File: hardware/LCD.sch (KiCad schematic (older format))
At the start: 31 parts, among them IC1 TPS61169DCKR, IC2 TPD4E001DRLR, IC3 AR1021-I/SS, U3 DS90CF364AMTD

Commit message: Assigning footprints
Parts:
- removed TOUCH1: HSMY-C170, EEZ DIB MCU r1B1:LED_0805, symbol LCD_PMOD-rescue:LED0805-EEZ_DIB_MCU_r1B2-eagle-import
- added TOUCH1: LED, LED_SMD:LED_0603_1608Metric, symbol antena:LED
- C1: footprint EEZ DIB MCU r1B1:C1206 -> Capacitor_SMD:C_1206_3216Metric
- C10, C11, C12, C13, C14, C15, C16, C9: renamed from C?; footprint (none) -> Capacitor_SMD:C_0603_1608Metric
- C2, C7: footprint EEZ DIB MCU r1B1:C0603 -> Capacitor_SMD:C_0603_1608Metric
- C3, C4, C5, C6, C8: footprint EEZ DIB MCU r1B1:C0805 -> Capacitor_SMD:C_0805_2012Metric
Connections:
- net 3V3: now also C2.2, C5.1, C7.2, C8.2, IC2.6 (VCC), IC3.1 (VDD), LCD_OUT1.4 (VDD), R3.2
- net 5V: now reaches C1.1, L1.1, R1.1
- net at R5.1: now also TOUCH1.2 (A)
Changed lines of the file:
@@
 	3300 1100 3400 1100
 Wire Wire Line
-	4600 2000 3900 2000
+	4600 2000 4550 2000
 Wire Wire Line
 	3900 2000 3900 1100
@@
 F 0 "C1" H 1415 1310 59  0000 R TNN
 F 1 "4u7" H 1415 1235 59  0000 R TNN
-F 2 "EEZ DIB MCU r1B1:C1206" H 1500 1300 50  0001 C CNN
+F 2 "Capacitor_SMD:C_1206_3216Metric" H 1500 1300 50  0001 C CNN
 F 3 "" H 1500 1300 50  0001 C CNN
 	1    1500 1300
@@
 F 0 "C3" H 3315 1335 59  0000 R TNN
 F 1 "1u" H 3315 1235 59  0000 R TNN
-F 2 "EEZ DIB MCU r1B1:C0805" H 3400 1300 50  0001 C CNN
+F 2 "Capacitor_SMD:C_0805_2012Metric" H 3400 1300 50  0001 C CNN
 F 3 "" H 3400 1300 50  0001 C CNN
 	1    3400 1300
@@
 F 0 "C4" H 3515 6235 59  0000 R TNN
 F 1 "10n" H 3515 6135 59  0000 R TNN
-F 2 "EEZ DIB MCU r1B1:C0805" H 3600 6200 50  0001 C CNN
+F 2 "Capacitor_SMD:C_0805_2012Metric" H 3600 6200 50  0001 C CNN
 F 3 "" H 3600 6200 50  0001 C CNN
 	1    3600 6200
@@
 F 0 "C6" H 3915 6135 59  0000 R TNN
 F 1 "10n" H 3915 6035 59  0000 R TNN
-F 2 "EEZ DIB MCU r1B1:C0805" H 4000 6100 50  0001 C CNN
+F 2 "Capacitor_SMD:C_0805_2012Metric" H 4000 6100 50  0001 C CNN
 F 3 "" H 4000 6100 50  0001 C CNN
 	1    4000 6100
@@
 F 0 "C7" H 5810 5240 59  0000 L BNN
 F 1 "100n" H 5810 5460 59  0000 L TNN
-F 2 "EEZ DIB MCU r1B1:C0603" H 5800 5400 50  0001 C CNN
+F 2 "Capacitor_SMD:C_0603_1608Metric" H 5800 5400 50  0001 C CNN
 F 3 "" H 5800 5400 50  0001 C CNN
 	1    5800 5400
@@
 F 0 "C8" H 6090 5310 59  0000 R TNN
 F 1 "1u" H 6090 5460 59  0000 R TNN
-F 2 "EEZ DIB MCU r1B1:C0805" H 6100 5400 50  0001 C CNN
+F 2 "Capacitor_SMD:C_0805_2012Metric" H 6100 5400 50  0001 C CNN
 F 3 "" H 6100 5400 50  0001 C CNN
 	1    6100 5400
 	-1   0    0    1
-$EndComp
-$Comp
-L LCD_PMOD-rescue:+3V3-EEZ_DIB_MCU_r1B2-eagle-import #+3V?
-U 1 0 5E224EFC
-P 6100 4900
-AR Path="/5E224EFC" Ref="#+3V?"  Part="1"
-AR Path="/5B8E2134/5E224EFC" Ref="#+3V?"  Part="1"
-AR Path="/5E224865/5E224EFC" Ref="#+3V0101"  Part="1"
-F 0 "#+3V0101" H 6100 4900 50  0001 C CNN
-F 1 "+3V3" H 5975 4975 59  0000 L TNN
-F 2 "" H 6100 4900 50  0001 C CNN
-F 3 "" H 6100 4900 50  0001 C CNN
-	1    6100 4900
-	1    0    0    -1
-$EndComp
-$Comp
-L LCD_PMOD-rescue:+3V3-EEZ_DIB_MCU_r1B2-eagle-import #+3V?
-U 1 0 5E224F02
-P 3800 2000
-AR Path="/5E224F02" Ref="#+3V?"  Part="1"
-AR Path="/5B8E2134/5E224F02" Ref="#+3V?"  Part="1"
-AR Path="/5E224865/5E224F02" Ref="#+3V0102"  Part="1"
-F 0 "#+3V0102" H 3800 2000 50  0001 C CNN
-F 1 "+3V3" H 3975 2075 59  0000 R TNN
-F 2 "" H 3800 2000 50  0001 C CNN
-F 3 "" H 3800 2000 50  0001 C CNN
-	1    3800 2000
-	-1   0    0    -1
 $EndComp
 $Comp
@@
 	1    3200 1100
 	1    0    0    -1
-$EndComp
-$Comp
-L LCD_PMOD-rescue:+3V3-EEZ_DIB_MCU_r1B2-eagle-import #+3V?
-U 1 0 5E224F0F
-P 3100 3600
-AR Path="/5E224F0F" Ref="#+3V?"  Part="1"
-AR Path="/5B8E2134/5E224F0F" Ref="#+3V?"  Part="1"
-AR Path="/5E224865/5E224F0F" Ref="#+3V0103"  Part="1"
-F 0 "#+3V0103" H 3100 3600 50  0001 C CNN
-F 1 "+3V3" V 3175 3700 59  0000 R TNN
-F 2 "" H 3100 3600 50  0001 C CNN
-F 3 "" H 3100 3600 50  0001 C CNN
-	1    3100 3600
-	0    -1   -1   0
 $EndComp
 $Comp
@@
 F 0 "C5" H 3715 2265 59  0000 R BNN
 F 1 "2u2" H 3715 2190 59  0000 R BNN
-F 2 "EEZ DIB MCU r1B1:C0805" H 3800 2300 50  0001 C CNN
+F 2 "Capacitor_SMD:C_0805_2012Metric" H 3800 2300 50  0001 C CNN
 F 3 "" H 3800 2300 50  0001 C CNN
 	1    3800 2300
@@
 $EndComp
 $Comp
-L LCD_PMOD-rescue:+3V3-EEZ_DIB_MCU_r1B2-eagle-import #+3V?
-U 1 0 5E224F31
-P 2100 5200
-AR Path="/5E224F31" Ref="#+3V?"  Part="1"
-AR Path="/5B8E2134/5E224F31" Ref="#+3V?"  Part="1"
-AR Path="/5E224865/5E224F31" Ref="#+3V0104"  Part="1"
-F 0 "#+3V0104" H 2100 5200 50  0001 C CNN
-F 1 "+3V3" H 2025 5225 59  0000 L BNN
-F 2 "" H 2100 5200 50  0001 C CNN
-F 3 "" H 2100 5200 50  0001 C CNN
-	1    2100 5200
-	-1   0    0    -1
-$EndComp
-$Comp
 L LCD_PMOD-rescue:C-EUC0603-EEZ_DIB_MCU_r1B2-eagle-import C?
 U 1 0 5E224F37
@@
 F 0 "C2" H 2185 5535 59  0000 L TNN
 F 1 "100n" H 2185 5610 59  0000 L TNN
-F 2 "EEZ DIB MCU r1B1:C0603" H 2100 5600 50  0001 C CNN
+F 2 "Capacitor_SMD:C_0603_1608Metric" H 2100 5600 50  0001 C CNN
 F 3 "" H 2100 5600 50  0001 C CNN
 	1    2100 5600
 	-1   0    0    1
-$EndComp
-$Comp
-L LCD_PMOD-rescue:LED0805-EEZ_DIB_MCU_r1B2-eagle-import TOUCH?
-U 1 0 5E224F3E
-P 6400 6400
-AR Path="/5E224F3E" Ref="TOUCH?"  Part="1"
-AR Path="/5B8E2134/5E224F3E" Ref="TOUCH?"  Part="1"
-AR Path="/5E224865/5E224F3E" Ref="TOUCH1"  Part="1"
-F 0 "TOUCH1" V 6365 6380 59  0000 R BNN
-F 1 "HSMY-C170" V 6550 6680 59  0000 R BNN
-F 2 "EEZ DIB MCU r1B1:LED_0805" H 6400 6400 50  0001 C CNN
-F 3 "" H 6400 6400 50  0001 C CNN
-	1    6400 6400
-	0    -1   1    0
 $EndComp
 $Comp
@@
 Connection ~ 4300 1900
 Wire Wire Line
-	4300 1900 4600 1900
+	4300 1900 4550 1900
 Text Label 3850 3700 0    50   ~ 0
 Touch_XR
@@
 Text Label 2625 1100 0    50   ~ 0
 VLED_SW
-$Comp
-L LCD_PMOD-rescue:+5V-EEZ_DIB_MCU_r1B2-eagle-import #P+?
-U 1 0 5E224FDA
-P 1300 1100
-AR Path="/5E224FDA" Ref="#P+?"  Part="1"
-AR Path="/5B8E2134/5E224FDA" Ref="#P+?"  Part="1"
-AR Path="/5E224865/5E224FDA" Ref="#P+0101"  Part="1"
-F 0 "#P+0101" H 1300 1100 50  0001 C CNN
-F 1 "+5V" V 1325 1125 59  0000 L BNN
-F 2 "" H 1300 1100 50  0001 C CNN
-F 3 "" H 1300 1100 50  0001 C CNN
-	1    1300 1100
-	0    -1   1    0
-$EndComp
 $Comp
 L DS90CF364AMTD:DS90CF364AMTD U3
@@
 P 9700 5900
 AR Path="/5E22D431/5E384C70" Ref="C?"  Part="1"
-AR Path="/5E224865/5E384C70" Ref="C?"  Part="1"
-F 0 "C?" H 9815 5946 50  0000 L CNN
+AR Path="/5E224865/5E384C70" Ref="C13"  Part="1"
+F 0 "C13" H 9815 5946 50  0000 L CNN
 F 1 "100n" H 9815 5855 50  0000 L CNN
-F 2 "" H 9738 5750 50  0001 C CNN
+F 2 "Capacitor_SMD:C_0603_1608Metric" H 9738 5750 50  0001 C CNN
 F 3 "~" H 9700 5900 50  0001 C CNN
 	1    9700 5900
@@
 P 10100 5900
 AR Path="/5E22D431/5E384C7B" Ref="C?"  Part="1"
-AR Path="/5E224865/5E384C7B" Ref="C?"  Part="1"
-F 0 "C?" H 10215 5946 50  0000 L CNN
+AR Path="/5E224865/5E384C7B" Ref="C14"  Part="1"
+F 0 "C14" H 10215 5946 50  0000 L CNN
 F 1 "100n" H 10215 5855 50  0000 L CNN
-F 2 "" H 10138 5750 50  0001 C CNN
+F 2 "Capacitor_SMD:C_0603_1608Metric" H 10138 5750 50  0001 C CNN
 F 3 "~" H 10100 5900 50  0001 C CNN
 	1    10100 5900
@@
 P 10500 5900
 AR Path="/5E22D431/5E384C86" Ref="C?"  Part="1"
-AR Path="/5E224865/5E384C86" Ref="C?"  Part="1"
-F 0 "C?" H 10615 5946 50  0000 L CNN
+AR Path="/5E224865/5E384C86" Ref="C15"  Part="1"
+F 0 "C15" H 10615 5946 50  0000 L CNN
 F 1 "100n" H 10615 5855 50  0000 L CNN
-F 2 "" H 10538 5750 50  0001 C CNN
+F 2 "Capacitor_SMD:C_0603_1608Metric" H 10538 5750 50  0001 C CNN
 F 3 "~" H 10500 5900 50  0001 C CNN
 	1    10500 5900
@@
 P 10900 5900
 AR Path="/5E22D431/5E384C91" Ref="C?"  Part="1"
-AR Path="/5E224865/5E384C91" Ref="C?"  Part="1"
-F 0 "C?" H 11015 5946 50  0000 L CNN
+AR Path="/5E224865/5E384C91" Ref="C16"  Part="1"
+F 0 "C16" H 11015 5946 50  0000 L CNN
 F 1 "100n" H 11015 5855 50  0000 L CNN
-F 2 "" H 10938 5750 50  0001 C CNN
+F 2 "Capacitor_SMD:C_0603_1608Metric" H 10938 5750 50  0001 C CNN
 F 3 "~" H 10900 5900 50  0001 C CNN
 	1    10900 5900
@@
 P 8050 5900
 AR Path="/5E22D431/5E384C9C" Ref="C?"  Part="1"
-AR Path="/5E224865/5E384C9C" Ref="C?"  Part="1"
-F 0 "C?" H 8165 5946 50  0000 L CNN
+AR Path="/5E224865/5E384C9C" Ref="C9"  Part="1"
+F 0 "C9" H 8165 5946 50  0000 L CNN
 F 1 "100n" H 8165 5855 50  0000 L CNN
-F 2 "" H 8088 5750 50  0001 C CNN
+F 2 "Capacitor_SMD:C_0603_1608Metric" H 8088 5750 50  0001 C CNN
 F 3 "~" H 8050 5900 50  0001 C CNN
 	1    8050 5900
@@
 P 8450 5900
 AR Path="/5E22D431/5E384CA7" Ref="C?"  Part="1"
-AR Path="/5E224865/5E384CA7" Ref="C?"  Part="1"
-F 0 "C?" H 8565 5946 50  0000 L CNN
+AR Path="/5E224865/5E384CA7" Ref="C10"  Part="1"
+F 0 "C10" H 8565 5946 50  0000 L CNN
 F 1 "100n" H 8565 5855 50  0000 L CNN
-F 2 "" H 8488 5750 50  0001 C CNN
+F 2 "Capacitor_SMD:C_0603_1608Metric" H 8488 5750 50  0001 C CNN
 F 3 "~" H 8450 5900 50  0001 C CNN
 	1    8450 5900
@@
 P 8850 5900
 AR Path="/5E22D431/5E384CB2" Ref="C?"  Part="1"
-AR Path="/5E224865/5E384CB2" Ref="C?"  Part="1"
-F 0 "C?" H 8965 5946 50  0000 L CNN
+AR Path="/5E224865/5E384CB2" Ref="C11"  Part="1"
+F 0 "C11" H 8965 5946 50  0000 L CNN
 F 1 "100n" H 8965 5855 50  0000 L CNN
-F 2 "" H 8888 5750 50  0001 C CNN
+F 2 "Capacitor_SMD:C_0603_1608Metric" H 8888 5750 50  0001 C CNN
 F 3 "~" H 8850 5900 50  0001 C CNN
 	1    8850 5900
@@
 P 9250 5900
 AR Path="/5E22D431/5E384CBD" Ref="C?"  Part="1"
-AR Path="/5E224865/5E384CBD" Ref="C?"  Part="1"
-F 0 "C?" H 9365 5946 50  0000 L CNN
+AR Path="/5E224865/5E384CBD" Ref="C12"  Part="1"
+F 0 "C12" H 9365 5946 50  0000 L CNN
 F 1 "100n" H 9365 5855 50  0000 L CNN
-F 2 "" H 9288 5750 50  0001 C CNN
+F 2 "Capacitor_SMD:C_0603_1608Metric" H 9288 5750 50  0001 C CNN
 F 3 "~" H 9250 5900 50  0001 C CNN
 	1    9250 5900
@@
 Text GLabel 1800 1800 0    50   Input ~ 0
 TFT_BRIGHTNESS
+Text GLabel 3800 2100 1    50   Input ~ 0
+3V3
+Text GLabel 6100 5000 1    50   Input ~ 0
+3V3
+Text GLabel 2100 5300 1    50   Input ~ 0
+3V3
+Text GLabel 3200 3600 0    50   Input ~ 0
+3V3
+Text GLabel 4550 1800 1    50   Input ~ 0
+VLED-
+Wire Wire Line
+	4550 1800 4550 1900
+Connection ~ 4550 1900
+Wire Wire Line
+	4550 1900 4600 1900
+Text GLabel 4450 2100 0    50   Input ~ 0
+VLED+
+Wire Wire Line
+	4450 2100 4550 2100
+Wire Wire Line
+	4550 2100 4550 2000
 Wire Bus Line
 	6175 2700 6175 3200
@@
 Wire Bus Line
 	6175 1900 6175 2400
+Connection ~ 4550 2000
+Wire Wire Line
+	4550 2000 3900 2000
+Text GLabel 1400 1100 0    50   Input ~ 0
+5V
+$Comp
+L antena:LED TOUCH1
+U 1 1 5E2FA3FE
+P 6350 6400
+F 0 "TOUCH1" H 6342 6145 50  0000 C CNN
+F 1 "LED" H 6342 6236 50  0000 C CNN
+F 2 "LED_SMD:LED_0603_1608Metric" H 6350 6400 50  0001 C CNN
+F 3 "~" H 6350 6400 50  0001 C CNN
+	1    6350 6400
+	-1   0    0    1
+$EndComp
 $EndSCHEMATC

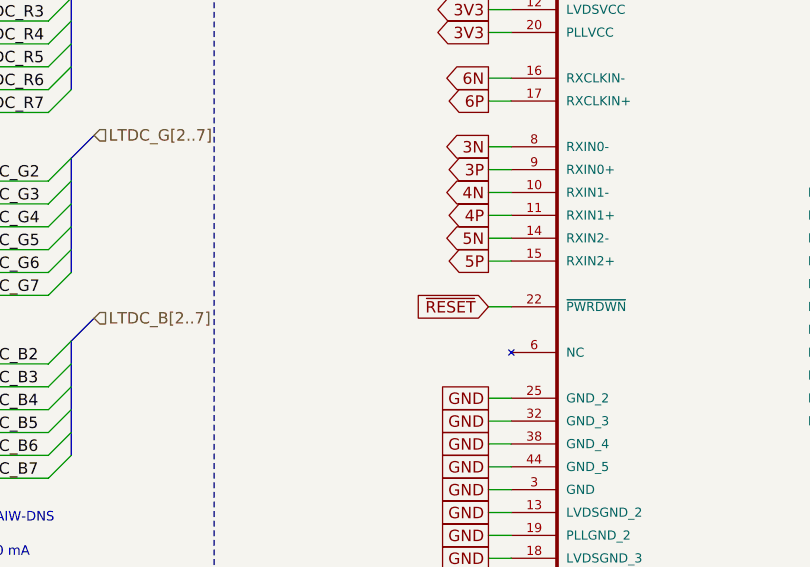
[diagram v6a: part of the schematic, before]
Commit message: Adding chip power down fix - removing ADS8556 chip
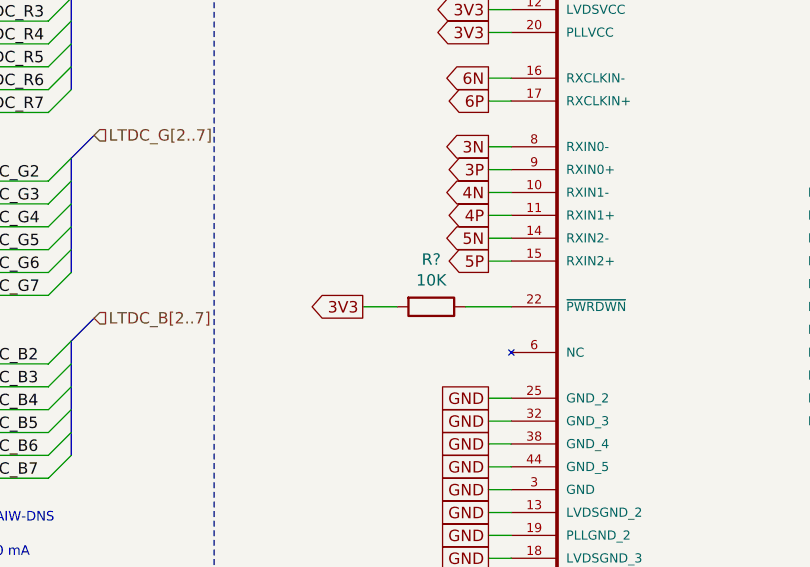
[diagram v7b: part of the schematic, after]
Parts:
- added R?: 10K, symbol antena:R
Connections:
- net 3V3: now also R?.2
- net ~RESET: no longer U3.22 (~PWRDWN)
- new net: R?.1, U3.22 (~PWRDWN)
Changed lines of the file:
@@
 Wire Wire Line
 	8000 2050 8100 2050
-Wire Wire Line
-	8000 3350 8100 3350
-Text GLabel 8000 3350 0    50   Input ~ 0
-~RESET
 Text GLabel 9700 5650 1    50   Input ~ 0
 3V3
@@
 Wire Wire Line
 	4550 2100 4550 2000
-Wire Bus Line
-	6175 2700 6175 3200
-Wire Bus Line
-	6175 3500 6175 4000
-Wire Bus Line
-	6175 1900 6175 2400
 Connection ~ 4550 2000
 Wire Wire Line
@@
 	-1   0    0    1
 $EndComp
+$Comp
+L antena:R R?
+U 1 1 5E356688
+P 7750 3350
+F 0 "R?" V 7543 3350 50  0000 C CNN
+F 1 "10K" V 7634 3350 50  0000 C CNN
+F 2 "" V 7680 3350 50  0001 C CNN
+F 3 "~" H 7750 3350 50  0001 C CNN
+	1    7750 3350
+	0    1    1    0
+$EndComp
+Text GLabel 7450 3350 0    50   Output ~ 0
+3V3
+Wire Wire Line
+	7900 3350 8100 3350
+Wire Wire Line
+	7450 3350 7600 3350
+Wire Bus Line
+	6175 2700 6175 3200
+Wire Bus Line
+	6175 3500 6175 4000
+Wire Bus Line
+	6175 1900 6175 2400
 $EndSCHEMATC
